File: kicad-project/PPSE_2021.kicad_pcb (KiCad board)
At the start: 2 copper layers, 100 x 60 mm, 133 parts, among them J1 Conn_02x04_Counter_Clockwise, J10 Motor 2, J11 Panel+ Connector, J2 Conn_02x08_Counter_Clockwise, J3 USB_B_Mini, J4 12V IN, J5 Compass, J6 Accelerometer, J7 OLED, J8 Panel- Connector, J9 Motor 1, Q1 3LP01M, Q10 SI2300DS, Q11 SI2300DS, Q12 SI2300DS, Q13 SI2300DS, Q2 PDTC114Y, Q3 BC846A, Q4 BC846A, Q5 BC846A, Q6 SI2300DS, Q7 SI2300DS, Q8 SI2300DS, Q9 SI2300DS, SW1 PRG_SW, SW2 RST_SW, SW3 HOME_SW, SW4 EN_SW, U1 W25Q16JVSS, U2 RP2040, U3 TPS563201, U4 PAM-7Q-0, Y1 12MHz

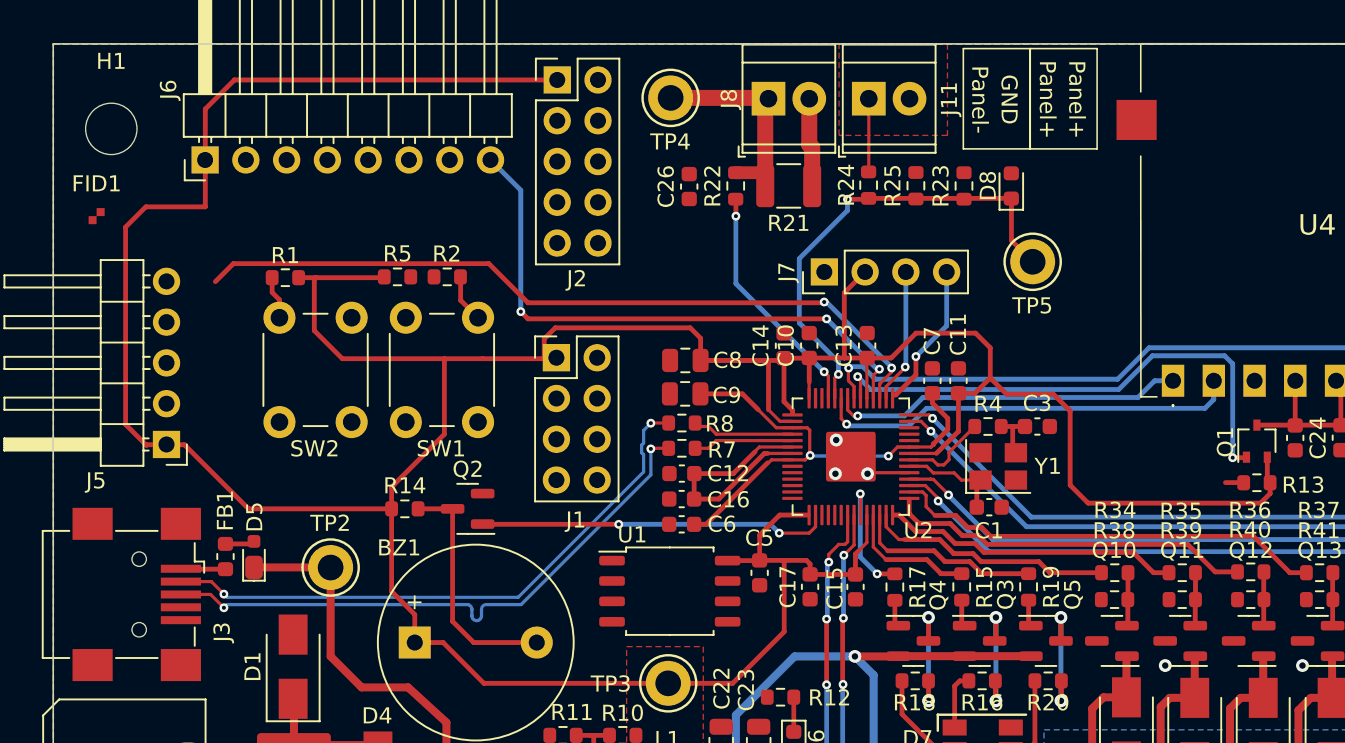
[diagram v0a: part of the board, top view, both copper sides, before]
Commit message: hw: finalize routing (dbg uart missing)
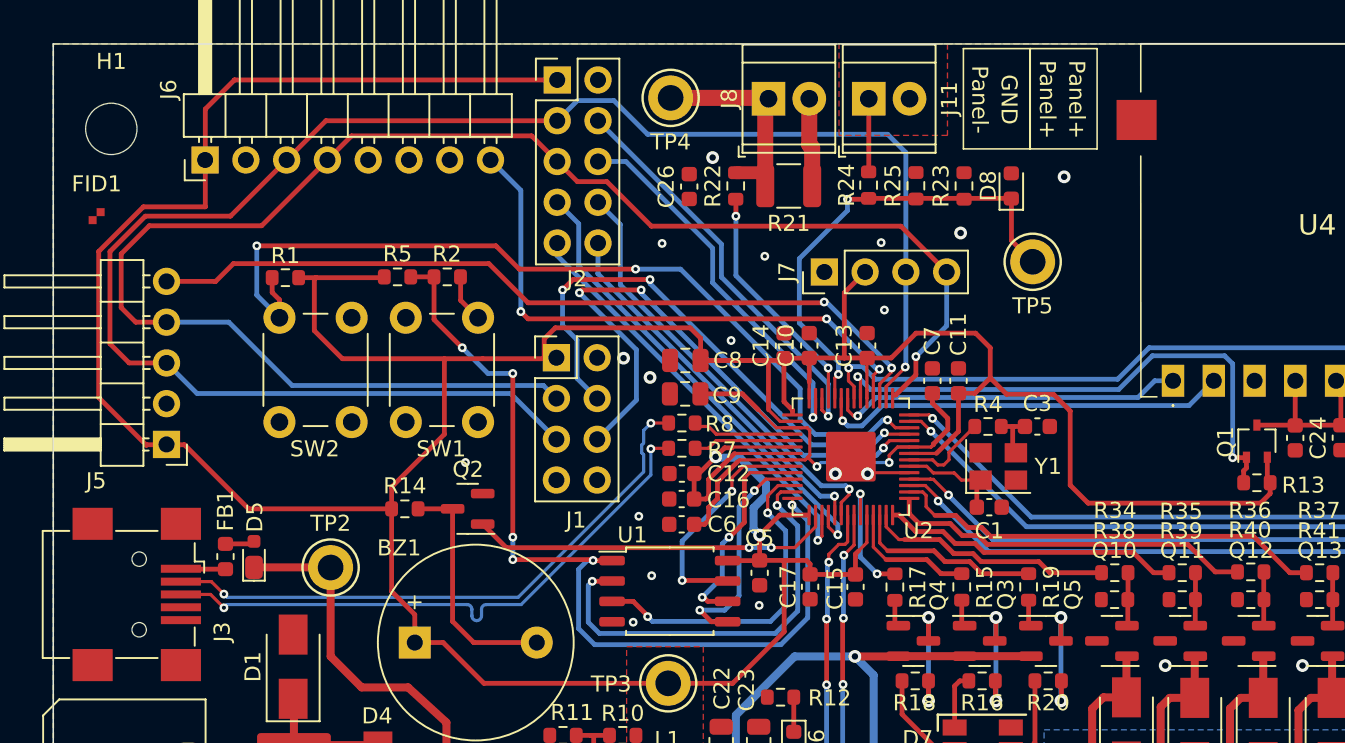
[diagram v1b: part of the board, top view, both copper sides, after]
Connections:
- J1 pad 2: /Control/SWCLK -> GND
- J1 pad 3: /Control/SWDIO -> /Connectivity/SDA
- J1 pad 4: GND -> /Control/SWDIO
- J1 pad 6: /Connectivity/SDA -> /Control/SWCLK
- J1 pad 7: /Connectivity/GPS_TX -> /Connectivity/GPS_RX
- J1 pad 8: /Connectivity/GPS_RX -> /Connectivity/GPS_TX
- J2 pad 10: /Control/EXT_ADC0 -> /Control/GPIO3
- J2 pad 2: /Control/GPIO4 -> GND
- J2 pad 3: GND -> /Connectivity/SCL
- J2 pad 4: /Control/GPIO3 -> /Control/EXT_ADC0
- J2 pad 5: /Connectivity/SCL -> /Connectivity/SDA
- J2 pad 6: /Control/GPIO2 -> /Control/EXT_ADC1
- J2 pad 7: /Connectivity/SDA -> /Control/GPIO2
- J2 pad 8: /Control/GPIO1 -> /Control/GPIO4
- J2 pad 9: /Control/EXT_ADC1 -> /Control/GPIO1
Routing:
- net /Connectivity/SCL: track 8.38 -> 106.7 mm
- net /Connectivity/SDA: track 9.12 -> 99.9 mm
- net /Control/~{FLASH_CS}: track 0.00 -> 56.3 mm, vias 0 -> 6
- net /Control/~{RESET}: track 2.68 -> 55.0 mm, vias 0 -> 3
- net /Control/SWCLK: track 0.00 -> 37.0 mm, vias 0 -> 3
- net /Control/SWDIO: track 0.00 -> 34.3 mm, vias 0 -> 3
- net /Control/GPIO2: track 0.00 -> 29.5 mm, vias 0 -> 1
- net /Control/GPIO4: track 0.00 -> 27.1 mm, vias 0 -> 1
- net /Control/GPIO1: track 0.00 -> 26.9 mm, vias 0 -> 1
- net /Control/FLASH_D1: track 0.00 -> 26.6 mm, vias 0 -> 2
- net /Control/EXT_ADC0: track 0.00 -> 25.6 mm, vias 0 -> 1
- net /Control/EXT_ADC1: track 0.00 -> 23.8 mm, vias 0 -> 1
- net /Control/GPIO3: track 0.00 -> 23.7 mm, vias 0 -> 1
- net /Control/FLASH_D2: track 0.00 -> 20.9 mm, vias 0 -> 2
- net /Control/FLASH_D3: track 0.00 -> 14.6 mm, vias 0 -> 2
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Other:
- board text removed: "Cambiare se serve"

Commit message: hw: final changes
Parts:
- J1: value Conn_02x04_Counter_Clockwise -> Conn_02x03_Counter_Clockwise; footprint Connector_PinHeader_2.54mm:PinHeader_2x04_P2.54mm_Vertical -> Connector_PinHeader_2.54mm:PinHeader_2x03_P2.54mm_Vertical
- R23: value R -> R DNP
- moved FID2 3.43 mm to (183.4, 83.8)
- moved FID1 2.92 mm to (91.5, 83.0)
- moved J1 2.85 mm to (118.9, 97.3)
- moved H4 1.50 mm to (183.5, 78.9)
- moved H1 1.35 mm to (91.5, 78.9)
- moved H2 0.74 mm to (91.5, 130.9)
- moved FID3 0.41 mm to (183.4, 126.3)
- moved H3 0.37 mm to (183.5, 130.9)
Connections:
- U4 pad MP1: unconnected-(U4-PadMP1) -> GND
- U4 pad MP2: unconnected-(U4-PadMP2) -> GND
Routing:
- net +12V: track 68.6 -> 83.7 mm, vias 9 -> 8
- net /Connectivity/SDA: track 99.9 -> 104.8 mm
- net GND: track 8.27 -> 11.5 mm, vias 22 -> 49
- net /Connectivity/SCL: track 106.7 -> 108.7 mm
- net /Control/SWCLK: track 37.0 -> 35.1 mm
- net /Connectivity/ACC_INT: track 36.0 -> 34.2 mm, vias 3 -> 2
- net /Control/FLASH_D3: track 14.6 -> 13.0 mm
- net /Control/~{RESET}: track 55.0 -> 53.4 mm
- net +3V3: track 284.7 -> 283.2 mm
- net /Control/V_PANEL: track 29.5 -> 30.6 mm
- net /Control/~{FLASH_CS}: track 56.3 -> 55.6 mm
- net /Control/~{HOME_SW}: track 30.3 -> 30.2 mm, vias 3 -> 1
- net /Control/~{EN_SW}: vias 3 -> 1
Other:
- outline, holes or cut-outs redrawn
- board text added: "+"
- board text added: "+12V"
- board text added: "-"
- board text added: "1"
- board text added: "12V"
- board text added: "2"
- board text added: "2022-04-11 Rev 1.0"
- board text added: "209445 209386 209270 209002 209466"
- board text added: "3"
- board text added: "3V3"
- board text added: "4"
- board text added: "ACC"
- board text added: "ADC0"
- board text added: "ADC1"
- board text added: "Accelerometer"
- board text added: "BOT"
- board text added: "Compass"
- board text added: "DRDY"
- board text added: "Debug"
- board text added: "Expansion"
- board text added: "GPS"
- board text added: "IO1"
- board text added: "IO2"
- board text added: "IO3"
- board text added: "IO4"
- board text added: "Motor 1"
- board text added: "Motor 2"
- board text added: "Nonis Santarossa Canova Tollardo Berretta"
- board text added: "OLED"
- board text added: "RX"
- board text added: "SCL"
- board text added: "SDA"
- board text added: "SWCLK"
- board text added: "SWDIO"
- board text added: "SW_VIN"
- board text added: "Shunt"
- board text added: "Solar Azimuth and Longitude Motorized lOcator PPSE 2021/2022"
- board text added: "TP"
- board text added: "TX"
- board text added: "Thomas Lisa Tommaso Simone Gabriele"
- board text added: "V"
- board text added: "VCC"
- board text added: "V_BCKP"
- board text added: "V_Panel"
- board text added: "nc"
- board text removed: "BOTTOM"
- board text removed: "Controllare orientamento?"
- board text removed: "Difficile da saldare ->"

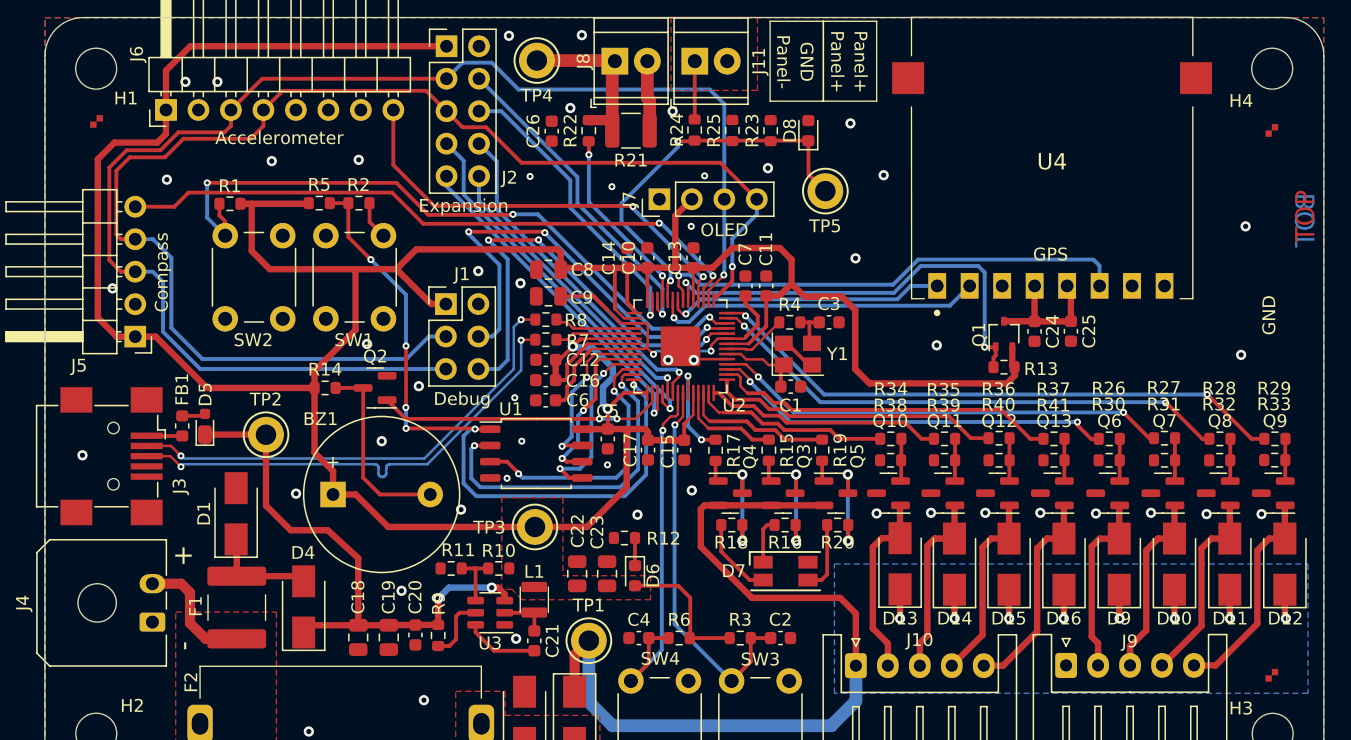
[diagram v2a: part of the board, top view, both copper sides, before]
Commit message: hw: small fixes to vias and silkscreen
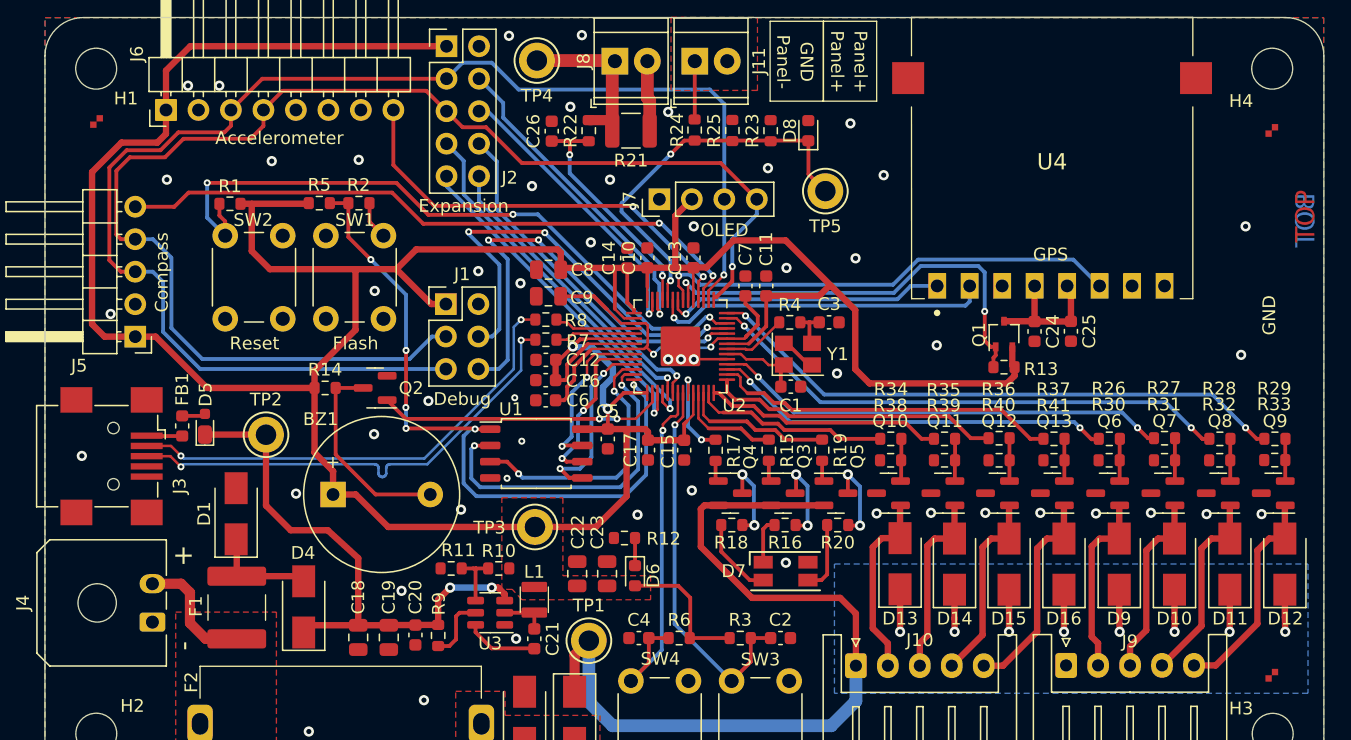
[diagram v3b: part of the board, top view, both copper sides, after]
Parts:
- moved C21 0.16 mm to (125.8, 123.5)
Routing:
- net +12V: track 83.7 -> 91.9 mm
- net /Control/I_PANEL: track 14.8 -> 18.8 mm
- net +3V3: track 283.2 -> 286.6 mm
- net Net-(Q4-Pad3): track 7.91 -> 6.78 mm
- net Net-(Q3-Pad3): track 7.96 -> 6.82 mm
- net Net-(Q5-Pad3): track 7.92 -> 6.80 mm
- net /Connectivity/iBuzzer: track 15.0 -> 16.0 mm
- net /Connectivity/GPS_TP: track 37.9 -> 37.0 mm
- net /Control/EXT_ADC1: track 23.8 -> 23.0 mm
- net /Connectivity/GPS_TX: track 25.9 -> 26.6 mm
- net /Control/LED_G: track 7.85 -> 7.25 mm
- net GND: vias 49 -> 52
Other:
- board text added: "Flash"
- board text added: "Reset"

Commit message: hw: add sensing resistance values
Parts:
- C26: value C -> 100n
- R22: value R -> 10k
- R23: value R DNP -> 4k7 DNP
- R24: value R -> 33k
- R25: value R -> 4k7
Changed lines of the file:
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@@
       (effects (font (size 1 1) (thickness 0.15)))
     )
-    (fp_text value "R" (at 0 1.43 90) (layer "F.Fab")
+    (fp_text value "33k" (at 0 1.43 90) (layer "F.Fab")
       (effects (font (size 1 1) (thickness 0.15)))
     )
@@
     (fp_line (start 0 -1.56) (end 0.65 -1.56) (layer "F.SilkS") (width 0.12))
     (fp_line (start 1.92 1.7) (end 1.92 -1.7) (layer "F.CrtYd") (width 0.05))
-    (fp_line (start -1.92 1.7) (end 1.92 1.7) (layer "F.CrtYd") (width 0.05))
     (fp_line (start 1.92 -1.7) (end -1.92 -1.7) (layer "F.CrtYd") (width 0.05))
+    (fp_line (start -1.92 1.7) (end 1.92 1.7) (layer "F.CrtYd") (width 0.05))
     (fp_line (start -1.92 -1.7) (end -1.92 1.7) (layer "F.CrtYd") (width 0.05))
+    (fp_line (start 0.65 -1.45) (end 0.65 1.45) (layer "F.Fab") (width 0.1))
     (fp_line (start -0.65 -1.125) (end -0.325 -1.45) (layer "F.Fab") (width 0.1))
-    (fp_line (start -0.65 1.45) (end -0.65 -1.125) (layer "F.Fab") (width 0.1))
     (fp_line (start 0.65 1.45) (end -0.65 1.45) (layer "F.Fab") (width 0.1))
-    (fp_line (start 0.65 -1.45) (end 0.65 1.45) (layer "F.Fab") (width 0.1))
     (fp_line (start -0.325 -1.45) (end 0.65 -1.45) (layer "F.Fab") (width 0.1))
+    (fp_line (start -0.65 1.45) (end -0.65 -1.125) (layer "F.Fab") (width 0.1))
     (pad "1" smd roundrect (at -0.9375 -0.95 180) (size 1.475 0.6) (layers "F.Cu" "F.Paste" "F.Mask") (roundrect_rratio 0.25)
       (net 75 "/Actuation/M2_OUT3") (pinfunction "D") (pintype "passive"))
@@
       (effects (font (size 1 1) (thickness 0.15)))
     )
-    (fp_text value "R DNP" (at 0 1.43 90) (layer "F.Fab")
+    (fp_text value "4k7 DNP" (at 0 1.43 90) (layer "F.Fab")
       (effects (font (size 1 1) (thickness 0.15)))
     )
@@
       (effects (font (size 1 1) (thickness 0.15)))
     )
-    (fp_text value "C" (at 0 1.43 90) (layer "F.Fab")
+    (fp_text value "100n" (at 0 1.43 90) (layer "F.Fab")
       (effects (font (size 1 1) (thickness 0.15)))
     )
@@
       (effects (font (size 1 1) (thickness 0.15)))
     )
-    (fp_text value "R" (at 0 1.43 90) (layer "F.Fab")
+    (fp_text value "4k7" (at 0 1.43 90) (layer "F.Fab")
       (effects (font (size 1 1) (thickness 0.15)))
     )
@@
       (effects (font (size 1 1) (thickness 0.15)))
     )
-    (fp_text value "R" (at 0 1.43 90) (layer "F.Fab")
+    (fp_text value "10k" (at 0 1.43 90) (layer "F.Fab")
       (effects (font (size 1 1) (thickness 0.15)))
     )
@@
     (pts (xy 187.5156 74.921538) (xy 187.5156 134.921538))
     (height -6.4388)
-    (gr_text "60,0000 mm" (at 192.1544 104.921538 90) (layer "Dwgs.User")
+    (gr_text "2362,2047 mils" (at 192.1544 104.921538 90) (layer "Dwgs.User")
       (effects (font (size 1.5 1.5) (thickness 0.3)))
     )
@@
     (pts (xy 87.5156 134.921538) (xy 187.5156 134.921538))
     (height 4.575262)
-    (gr_text "100,0000 mm" (at 137.5156 137.6968) (layer "Dwgs.User")
+    (gr_text "3937,0079 mils" (at 137.5156 137.6968) (layer "Dwgs.User")
       (effects (font (size 1.5 1.5) (thickness 0.3)))
     )

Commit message: hw: final pcb check before submit
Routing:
- net GND: vias 52 -> 55
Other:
- board text added: "SALMO"
- board text added: "Solar Azimuth and eLevation Motorized lOcator PPSE 2021/2022"
- board text removed: "Solar Azimuth and Longitude Motorized lOcator PPSE 2021/2022"
